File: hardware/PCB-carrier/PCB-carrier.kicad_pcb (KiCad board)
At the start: 4 copper layers, 24 x 95 mm, 8 parts

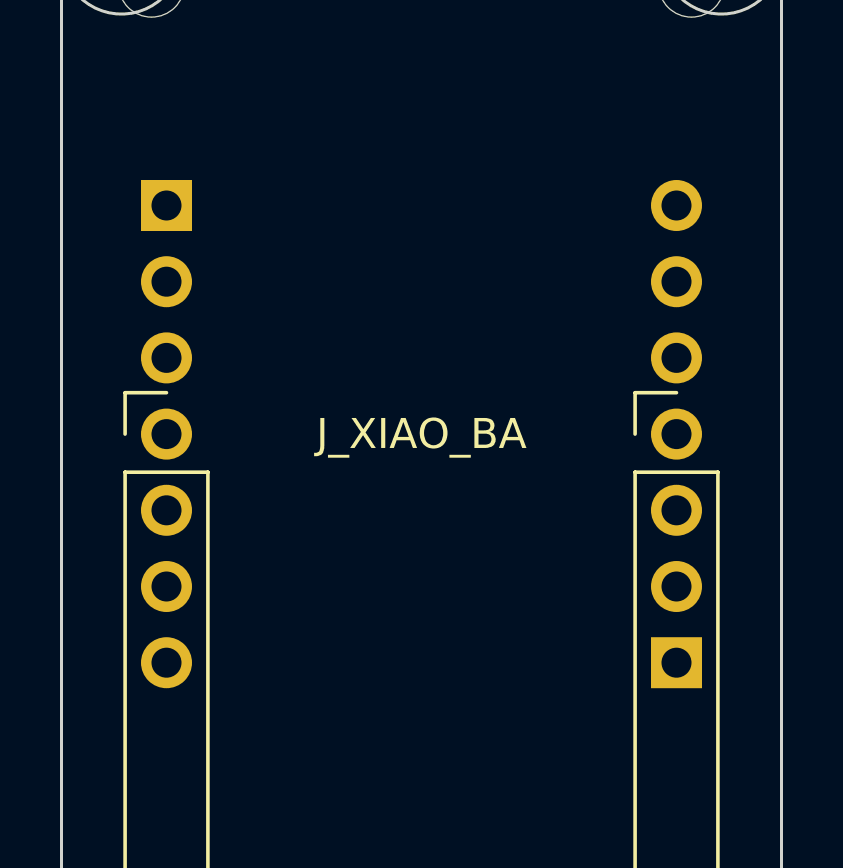
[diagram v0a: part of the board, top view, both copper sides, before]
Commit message: fix(carrier): net the bottom-face XIAO from its back, and draw the carrier
gen_carrier.py netted both XIAOs from one front-view pin table.
XIAO-ESP32S3-cam sits on the bottom face and presents its back to the
shared through-holes, so its rows were swapped: BUZZER on the 5V pin,
+3V3 and GND on D2 and D1, SDA/SCL on D9/D8. XIAO-ESP32S3-lora, on the
top face, was always right.

- Each XIAO's face is declared once (XIAO_*_FACE). add_xiao() mirrors x
  for the bottom face; y and the USB-C-aft orientation do not change.
  The cam's pins 1..7 move from the x = 3.5 row to 20.5.
- verify_pins() also checks every net against the underside-photo
  reading in module-pinouts.md, by signal name. Putting the face-blind
  add_xiao() back fails all five of the cam's nets.
- Board regenerated: DRC 0 violations, 0 unconnected. fab/gerbers/ is
  left alone -- it predates #18 and the rename, and belongs to #16.

New: gen_carrier_diagram.py draws PCB-carrier-layout.svg, both faces
dimensioned, from the board file and KiCad's XIAO footprint. It shows
the BAT pads and the pigtail exits (header plastic walls both long
sides, so a pigtail leaves through an end), and it refuses a board
whose rows disagree with the drawing. PCB-carrier.md embeds it.

XIAO-ESP32S3-cam.md: the pigtails leave through an open end, not past
a header row; plus the operator's BAT pad measurements.

Closes #21

Co-Authored-By: Claude Opus 5 (1M context) <noreply@anthropic.com>
Claude-Session: https://claude.ai/code/session_01VpmH8VC78J5DzhK9GC3Ujy
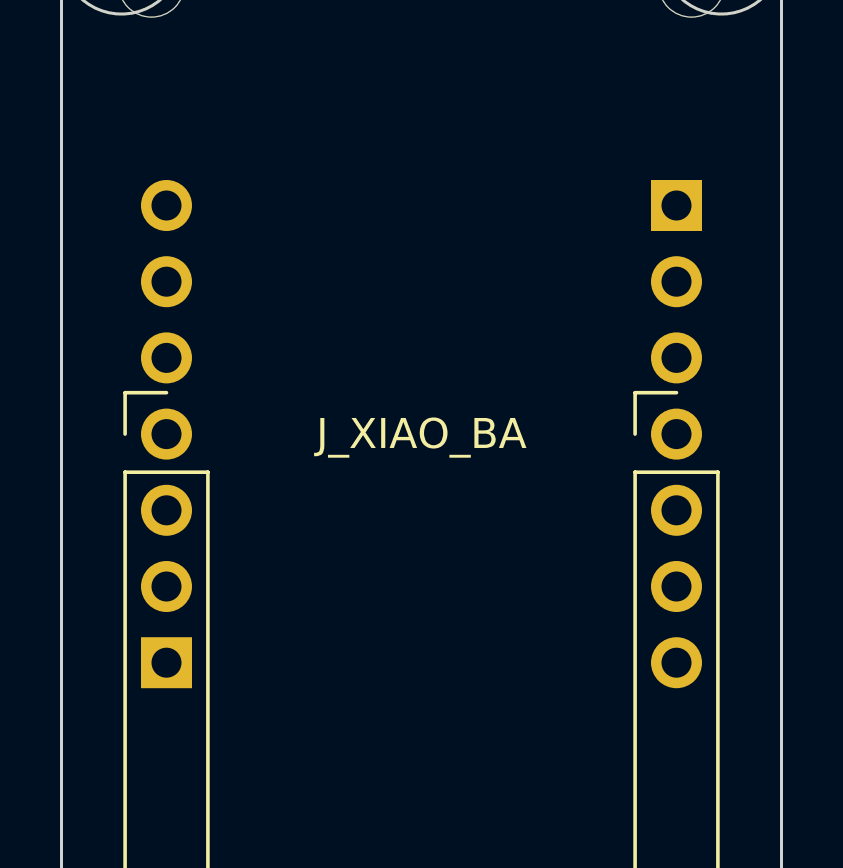
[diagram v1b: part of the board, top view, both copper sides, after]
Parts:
- moved J_XIAO_BA 17.0 mm to (20.5, 18.0)
- moved J_XIAO_BB 17.0 mm to (3.50, 18.0)

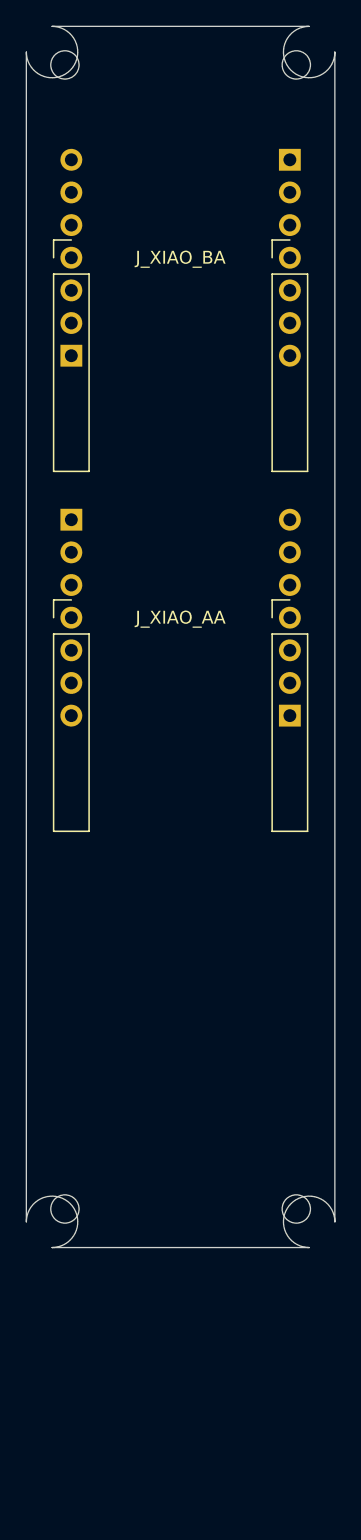
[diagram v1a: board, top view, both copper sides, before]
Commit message: feat(carrier)!: one two-sided board on the sled's centre line, hung off the web
The carrier as designed could never be fitted: the PayloadSled's web is
a solid 3 mm plate on the centre plane, and the 24 x 95 two-sided board
came from a camera-port drawing that put board and web in the same
place (#13). The operator's design (PCB-carrier-design.md):

- One board on the centre line. Tall side, facing 270 deg (camera):
  XIAO-ESP32S3-cam aft under the camera, the L76K-GNSS on its own pins,
  XIAO-ESP32S3-lora forward, the JST. Low side, facing 90 deg (web):
  LSM6DSO32 and BMP388 lengthwise, two Wuerth WA-SMSI M3 10 mm
  standoffs. 24 x 90.4 mm, ~4.1 g; the battery keeps its position.
- The web moves to r 10.5-13.5 toward 90 deg and the board hangs off
  it; M3 x 10 plastic screws from the web side (js-rocket#99).
- The sensors run lengthwise, rows 2.15 mm inboard of the modules'
  rows, and stand ~1 mm proud on their pins.
- One regulator per load: the cam XIAO feeds +3V3 and the sensors,
  the lora XIAO feeds only the L76K-GNSS on +3V3_LORA. BMP388 CS tied
  high (#19).

gen_carrier.py:
- verify_pins(): each XIAO against its underside photo, the L76K-GNSS
  by two routes, each back-side sensor by two routes (turn-then-mirror,
  mirror-then-turn). verify_clearances(): every through-hole against
  every other across both sides, plus standoffs and BMP388 legs. A
  mirrored L76K-GNSS, an unmirrored sensor and a sensor pin moved onto
  a module pin all fail the build.
- Header courtyards now sit over their pads (the old add_xiao() put
  them 7.62 mm off) and hug them; writes PCB-carrier.kicad_dru (the
  standoff land pattern's only exception) and PCB-carrier-layout.json.
- DRC 0 violations; 10 unconnected = the unrouted nets (#15).
- Footprints flipped to B.Cu only after they are on a board: Flip() on
  a detached footprint crashes pcbnew.

gen_carrier_diagram.py draws both sides from the JSON.

Docs: PCB-carrier.md and the design brief, README (interface,
connections), d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
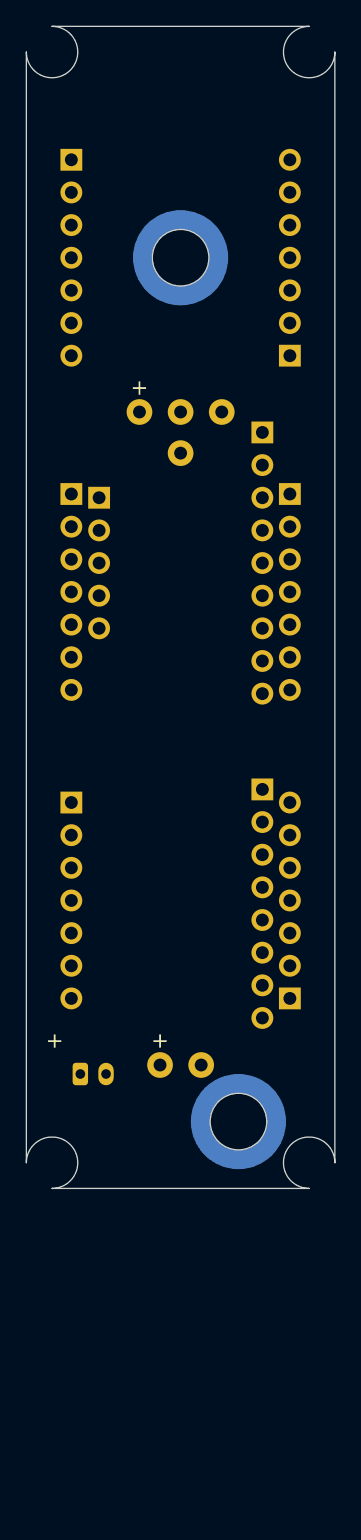
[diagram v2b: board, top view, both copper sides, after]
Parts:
- removed H1, H2, H3, H4: MountingHole_2.2mm_M2, MountingHole_2.2mm_M2
- removed J_XIAO_AA, J_XIAO_AB, J_XIAO_BA, J_XIAO_BB: PinHeader_1x07_P2.54mm_Vertical, PinHeader_1x07_P2.54mm_Vertical
- added J_BAT: JST_PH_S2B-PH-K_1x02_P2.00mm_Horizontal, JST_PH_S2B-PH-K_1x02_P2.00mm_Horizontal, F.Cu at (4.20, 81.5)
- added J_BMP: PinHeader_1x08_P2.54mm_Vertical, PinHeader_1x08_P2.54mm_Vertical, B.Cu at (18.4, 59.4)
- added J_CAM_A: PinHeader_1x07_P2.54mm_Vertical, PinHeader_1x07_P2.54mm_Vertical, F.Cu at (3.50, 10.4)
- added J_CAM_B: PinHeader_1x07_P2.54mm_Vertical, PinHeader_1x07_P2.54mm_Vertical, F.Cu at (20.5, 25.6)
- added J_L76K_A: PinHeader_1x07_P2.54mm_Vertical, PinHeader_1x07_P2.54mm_Vertical, F.Cu at (3.50, 36.4)
- added J_L76K_B: PinHeader_1x07_P2.54mm_Vertical, PinHeader_1x07_P2.54mm_Vertical, F.Cu at (20.5, 36.4)
- added J_LORA_A: PinHeader_1x07_P2.54mm_Vertical, PinHeader_1x07_P2.54mm_Vertical, F.Cu at (3.50, 60.4)
- added J_LORA_B: PinHeader_1x07_P2.54mm_Vertical, PinHeader_1x07_P2.54mm_Vertical, F.Cu at (20.5, 75.6)
- added J_LSM_A: PinHeader_1x05_P2.54mm_Vertical, PinHeader_1x05_P2.54mm_Vertical, B.Cu at (5.66, 36.7)
- added J_LSM_P: PinHeader_1x09_P2.54mm_Vertical, PinHeader_1x09_P2.54mm_Vertical, B.Cu at (18.4, 31.6)
- added SO1: Mounting_Wuerth_WA-SMSI-M3_H10mm_9774100360, Mounting_Wuerth_WA-SMSI-M3_H10mm_9774100360, B.Cu at (12.0, 18.0)
- added SO2: Mounting_Wuerth_WA-SMSI-M3_H10mm_9774100360, Mounting_Wuerth_WA-SMSI-M3_H10mm_9774100360, B.Cu at (16.5, 85.2)
- added TP_BUZ: TestPoint_THTPad_D2.0mm_Drill1.0mm, TestPoint_THTPad_D2.0mm_Drill1.0mm, F.Cu at (15.2, 30.0)
- added TP_BUZ_G: TestPoint_THTPad_D2.0mm_Drill1.0mm, TestPoint_THTPad_D2.0mm_Drill1.0mm, F.Cu at (12.0, 33.2)
- added TP_CAM_BAT_N: TestPoint_THTPad_D2.0mm_Drill1.0mm, TestPoint_THTPad_D2.0mm_Drill1.0mm, F.Cu at (12.0, 30.0)
- added TP_CAM_BAT_P: TestPoint_THTPad_D2.0mm_Drill1.0mm, TestPoint_THTPad_D2.0mm_Drill1.0mm, F.Cu at (8.80, 30.0)
- added TP_LORA_BAT_N: TestPoint_THTPad_D2.0mm_Drill1.0mm, TestPoint_THTPad_D2.0mm_Drill1.0mm, F.Cu at (13.6, 80.8)
- added TP_LORA_BAT_P: TestPoint_THTPad_D2.0mm_Drill1.0mm, TestPoint_THTPad_D2.0mm_Drill1.0mm, F.Cu at (10.4, 80.8)
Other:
- board size 24 x 95 mm -> 24 x 90.4 mm
- board text added: "+"

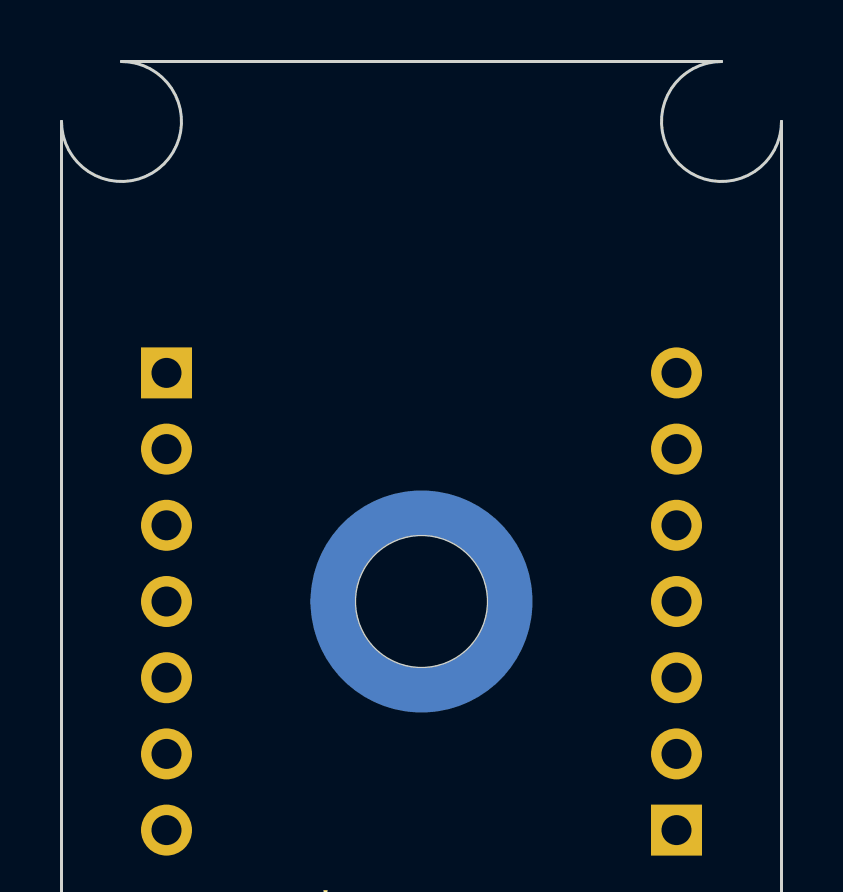
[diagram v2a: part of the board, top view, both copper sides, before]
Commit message: fix(carrier): standoff 1 to the board's aft end, clear of every module
It sat under XIAO-ESP32S3-cam, between the pin rows, where its 4.4 mm
board hole met the BAT pigtail in the gap under the XIAO, and a long
screw would have reached the XIAO's back (operator). Now at board
(12.0, 4.0), nose z 29.4, under the USB-C plug room: the hole spans
y 1.8-6.2, aft of the XIAO and its USB-C tab. Standoffs 81 mm apart;
the camera ~14 mm from standoff 1. DRC 0 violations.

The drawing now labels the other side's parts ("standoff, other side")
so a part behind the board no longer reads as a hole through a module.

Refs #22, jwilleke/js-rocket#99

Co-Authored-By: Claude Opus 5 <noreply@anthropic.com>
Claude-Session: https://claude.ai/code/session_01VpmH8VC78J5DzhK9GC3Ujy
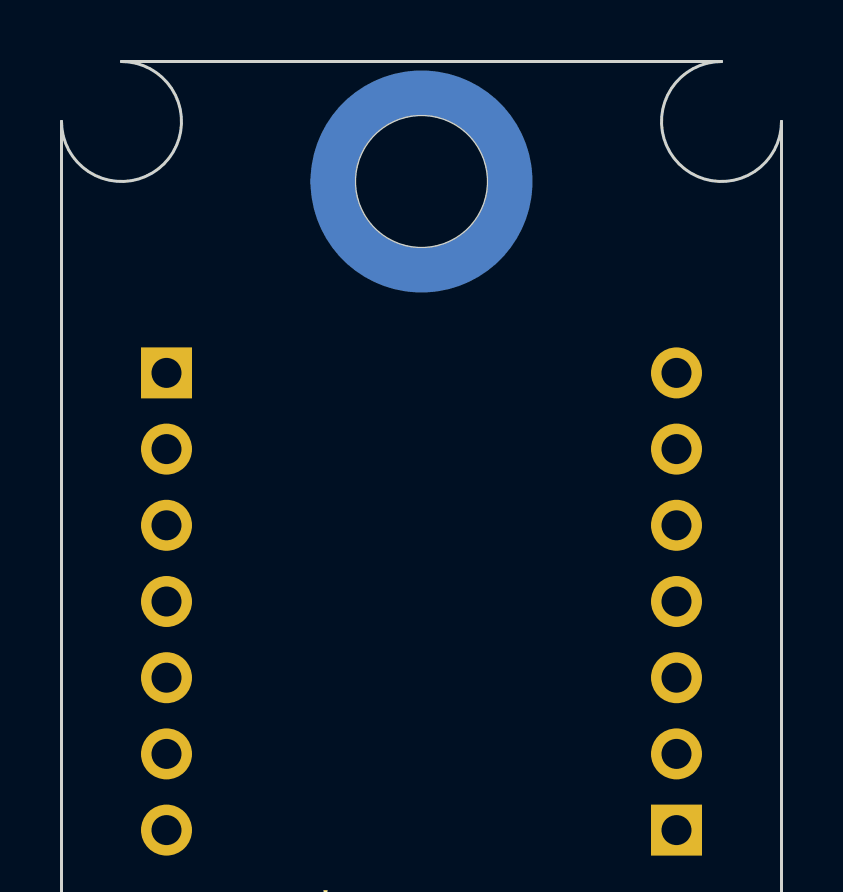
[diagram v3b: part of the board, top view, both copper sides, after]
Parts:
- moved SO1 14.0 mm to (12.0, 4.00)

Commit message: feat(carrier): label the XIAO battery-pigtail holes BAT + - on both sides (#14)
BAT_LABELS in gen_carrier.py puts BAT, + and - at each XIAO's pair of
pigtail holes on F.SilkS and, mirrored so it reads from the low side,
on B.SilkS -- the side the pigtails are soldered on (operator,
2026-09-13). Positions keep the text off every pad, the JST body and
standoff 2. The cam and lora "+" marks move from PLUS_MARKS into
BAT_LABELS; the JST's "+" stays. Board regenerated: DRC 0 violations,
10 unconnected (the unrouted signal nets, as before).

No CAM/LORA label: there was none on the board, and each pair sits
directly behind its own XIAO.

Refs #14

Co-Authored-By: Claude Opus 5 <noreply@anthropic.com>
Claude-Session: https://claude.ai/code/session_01VpmH8VC78J5DzhK9GC3Ujy
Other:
- board text added: "-"
- board text added: "BAT"

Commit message: feat(carrier): name each module on the board under it (#14)
MODULE_LABELS in gen_carrier.py puts each module's name on the
silkscreen under its outline, on its own side: XIAO-ESP32S3 / cam,
L76K-GNSS and XIAO-ESP32S3 / lora on the tall side; LSM6DSO32 and
BMP388 mirrored on the low side so they read from there. Centred between
each module's pin rows. Board regenerated; DRC at all severities: 0
violations, 10 unconnected (the unrouted signal nets). Checked by eye on
exported silkscreen for both sides.

Refs #14

Co-Authored-By: Claude Opus 5 <noreply@anthropic.com>
Claude-Session: https://claude.ai/code/session_01VpmH8VC78J5DzhK9GC3Ujy
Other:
- board text added: "BMP388"
- board text added: "L76K-GNSS"
- board text added: "LSM6DSO32"
- board text added: "XIAO-ESP32S3"
- board text added: "cam"
- board text added: "lora"

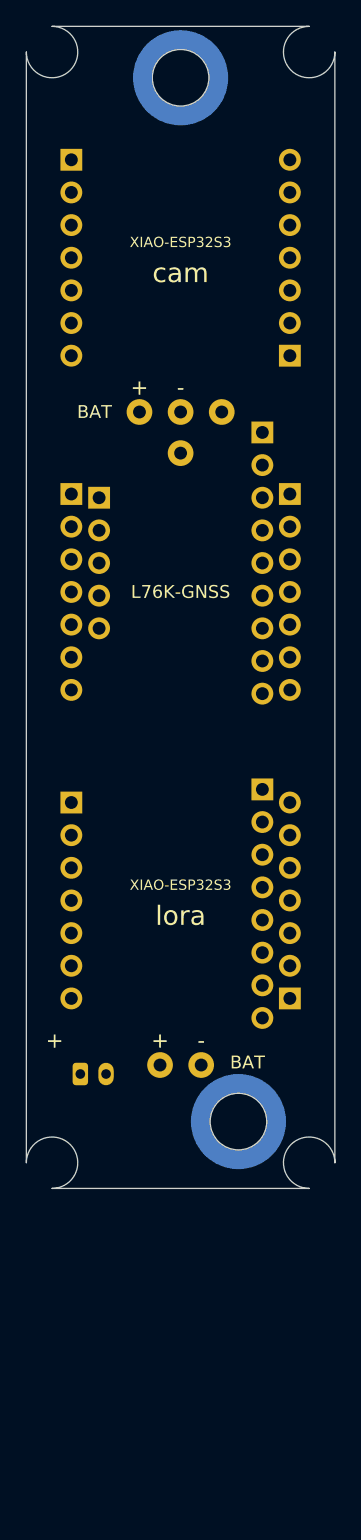
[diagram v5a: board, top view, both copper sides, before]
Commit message: feat(carrier): battery behind the board -- layout B2 in the generator
Operator chose B2, 2026-09-15. gen_carrier.py: board 90.4 -> 115.7 mm
(nose z 25.4-141.1), LSM6DSO32 aft to nose z 33.4-58.9, BMP388 forward to
107.25-132.75, forward standoff to (16.5, 110.5) = nose z 135.9, 5.2 mm
from the end and under no module. The battery lies on the low face between
them, nose z 70.5-106.5, on a 1 mm pad. verify_clearances passes (72
holes); kicad-cli DRC 0 violations, 10 unconnected (unrouted, as before).
Layout JSON and diagram regenerated. README, BOM (carrier est 5.2 g, nose
55.5 g), design, shopping list (~$40), LiPo, Antennas and the carrier pages
updated. Owed: stability, span stiffness over 106.5 mm, retention, pad,
charger placement, lead routing, GNSS patch.

Refs #22 #14

Co-Authored-By: Claude Opus 5 <noreply@anthropic.com>
Claude-Session: https://claude.ai/code/session_01VpmH8VC78J5DzhK9GC3Ujy
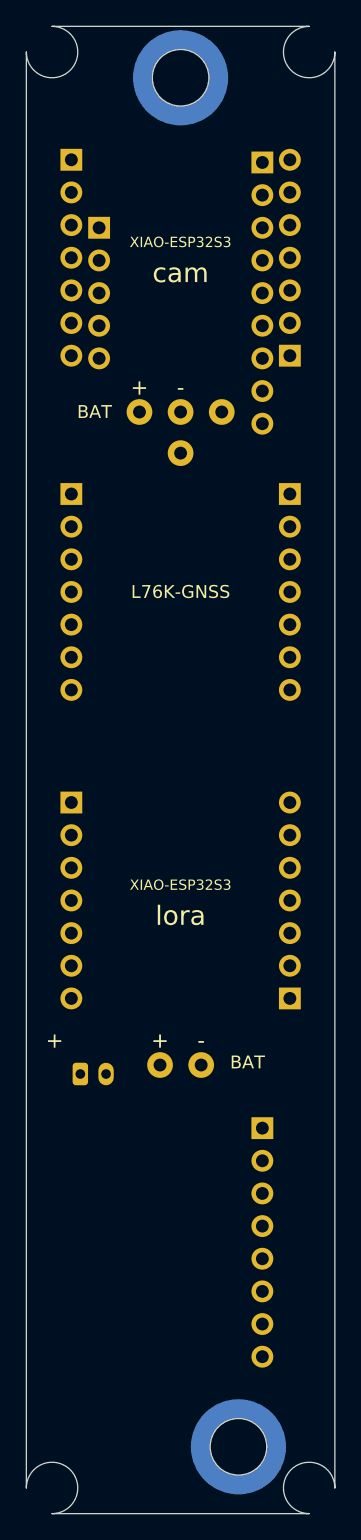
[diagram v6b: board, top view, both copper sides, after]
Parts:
- moved J_BMP 26.3 mm to (18.4, 85.7)
- moved SO2 25.3 mm to (16.5, 110.5)
- moved J_LSM_A 21.0 mm to (5.66, 15.7)
- moved J_LSM_P 21.0 mm to (18.4, 10.6)
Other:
- board size 24 x 90.4 mm -> 24 x 115.7 mm
